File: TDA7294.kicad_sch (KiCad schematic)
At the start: 16 parts, among them J1 PAWER, J2 OUT, J3 IN

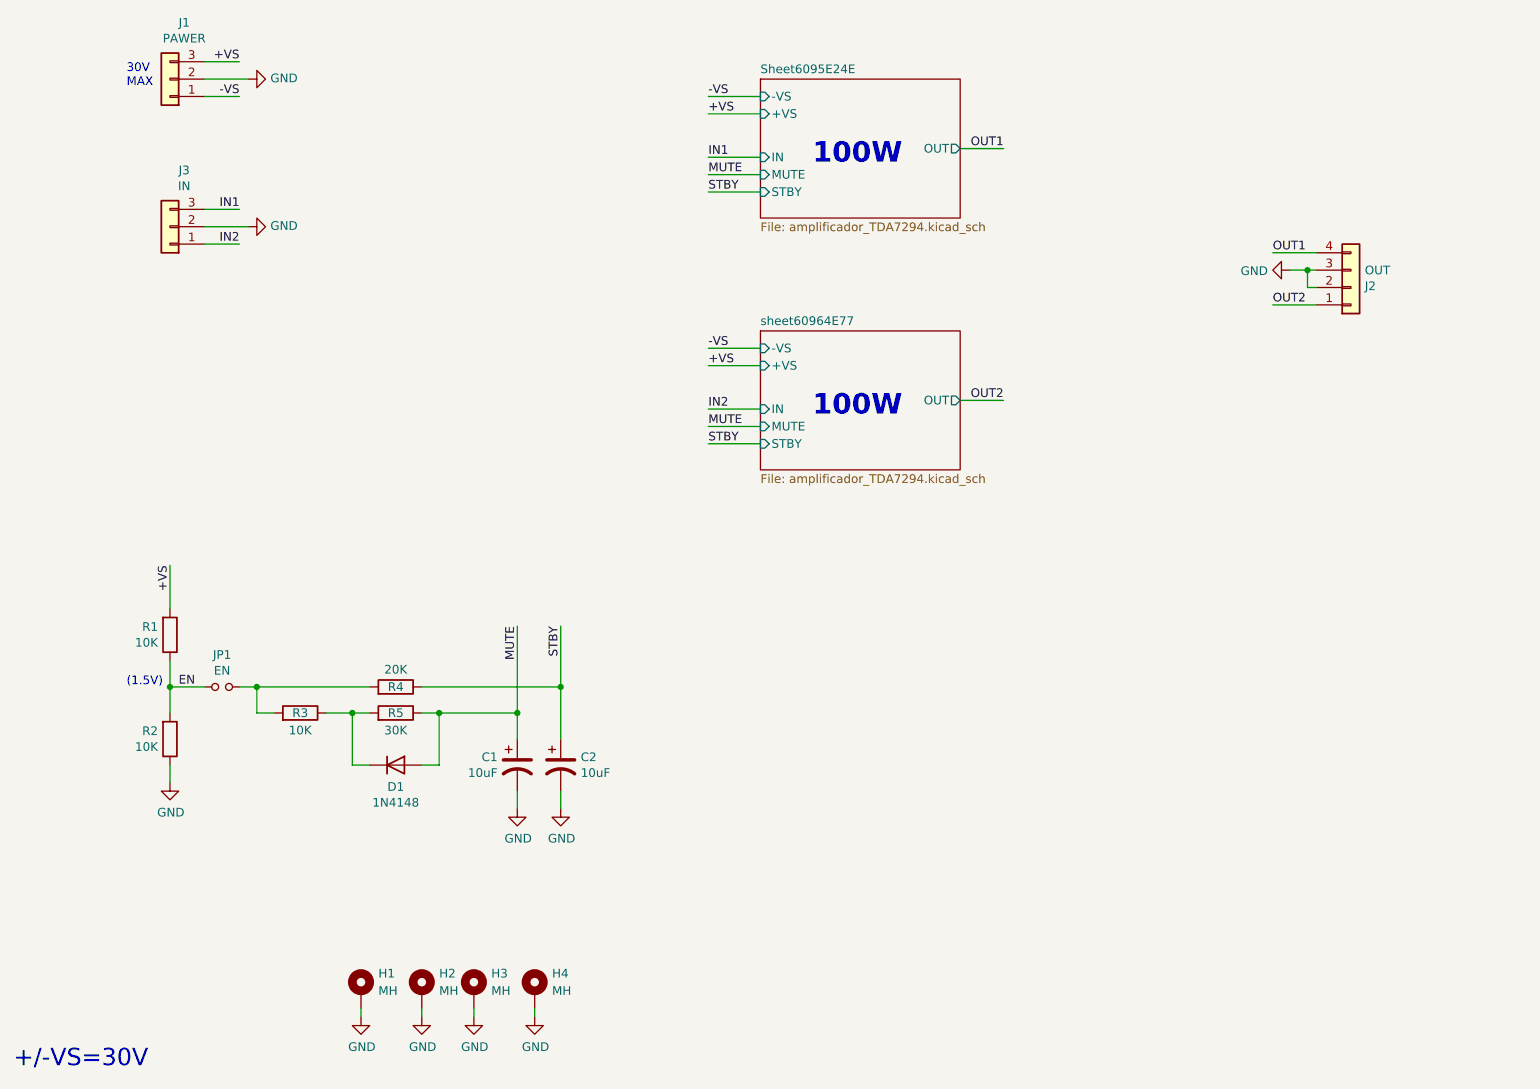
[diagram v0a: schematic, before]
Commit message: add version puenteable y archivos en pdf
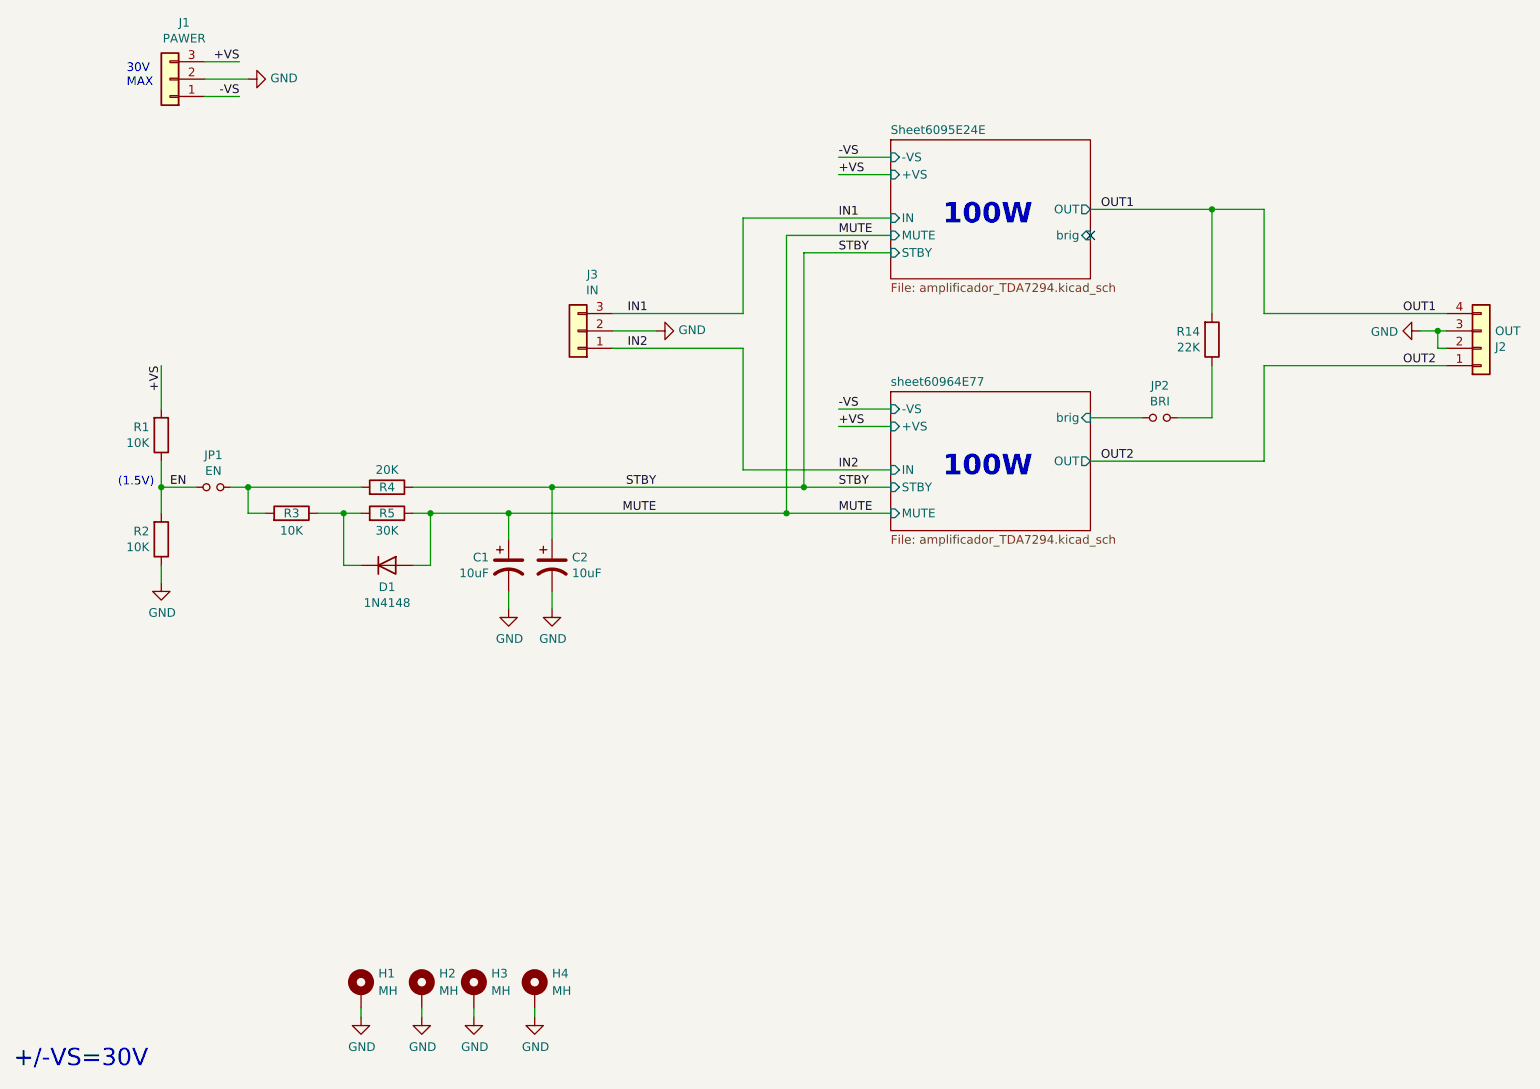
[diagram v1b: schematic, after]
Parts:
- added JP2: BRI, Connector_PinHeader_2.54mm:PinHeader_1x02_P2.54mm_Vertical, symbol TDA7294-rescue:Jumper_NO_Small-Device
- added R14: 22K, Resistor_THT:R_Axial_DIN0207_L6.3mm_D2.5mm_P10.16mm_Horizontal, symbol Device:R
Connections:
- net OUT1: now also R14.2
- new net: JP2.2, R14.1
- new net sheet60964E77/brig: JP2.1
- no-connect marks 0 -> 1
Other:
- sheet Sheet6095E24E ports: added brig; removed none
- sheet sheet60964E77 ports: added brig; removed none
- moved on the sheet: C1, C2, D1, J2, J3, JP1, R1, R2, R3, R4, R5
